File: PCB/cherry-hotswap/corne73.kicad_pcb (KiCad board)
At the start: 2 copper layers, 277.2 x 107.5 mm, 70 parts, among them J1 TYPE-C-31-M-13C, J2 TRS, J3 Conn_01x04, J4 Conn_01x03, SW1 SW_Push, SW10 SW_Push, SW11 SW_Push, SW12 SW_Push, SW13 SW_Push, SW14 SW_Push, SW15 SW_Push, SW16 SW_Push, SW17 SW_Push, SW18 SW_Push, SW19 SW_Push, SW2 SW_Push, SW20 SW_Push, SW21 SW_Push, SW3 SW_Push, SW4 SW_Push, SW5 SW_Push, SW6 SW_Push, SW7 SW_Push, SW8 SW_Push, SW9 SW_Push, U3 TPD4E05U06DQAR

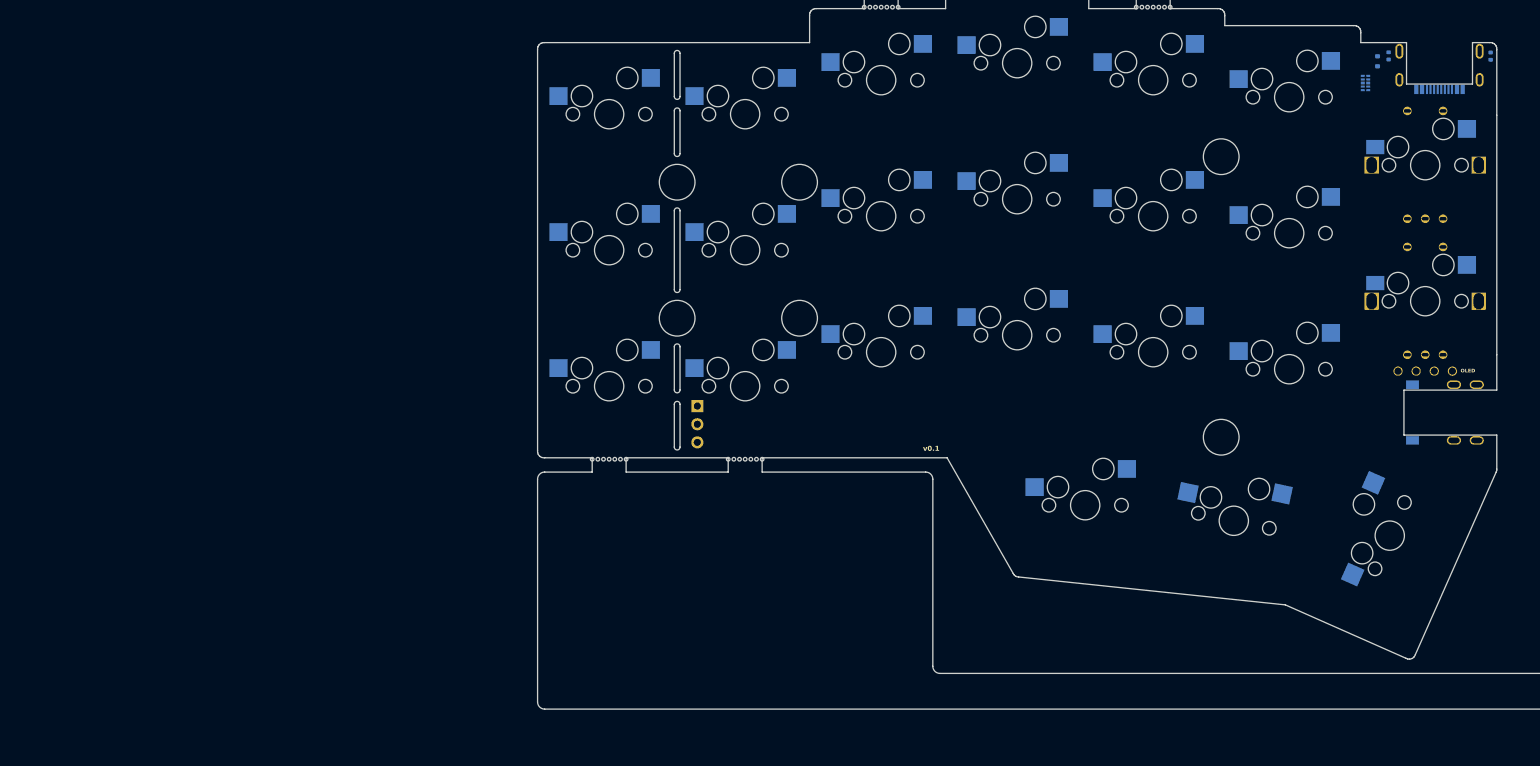
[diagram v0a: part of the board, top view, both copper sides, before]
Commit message: Initial left side components
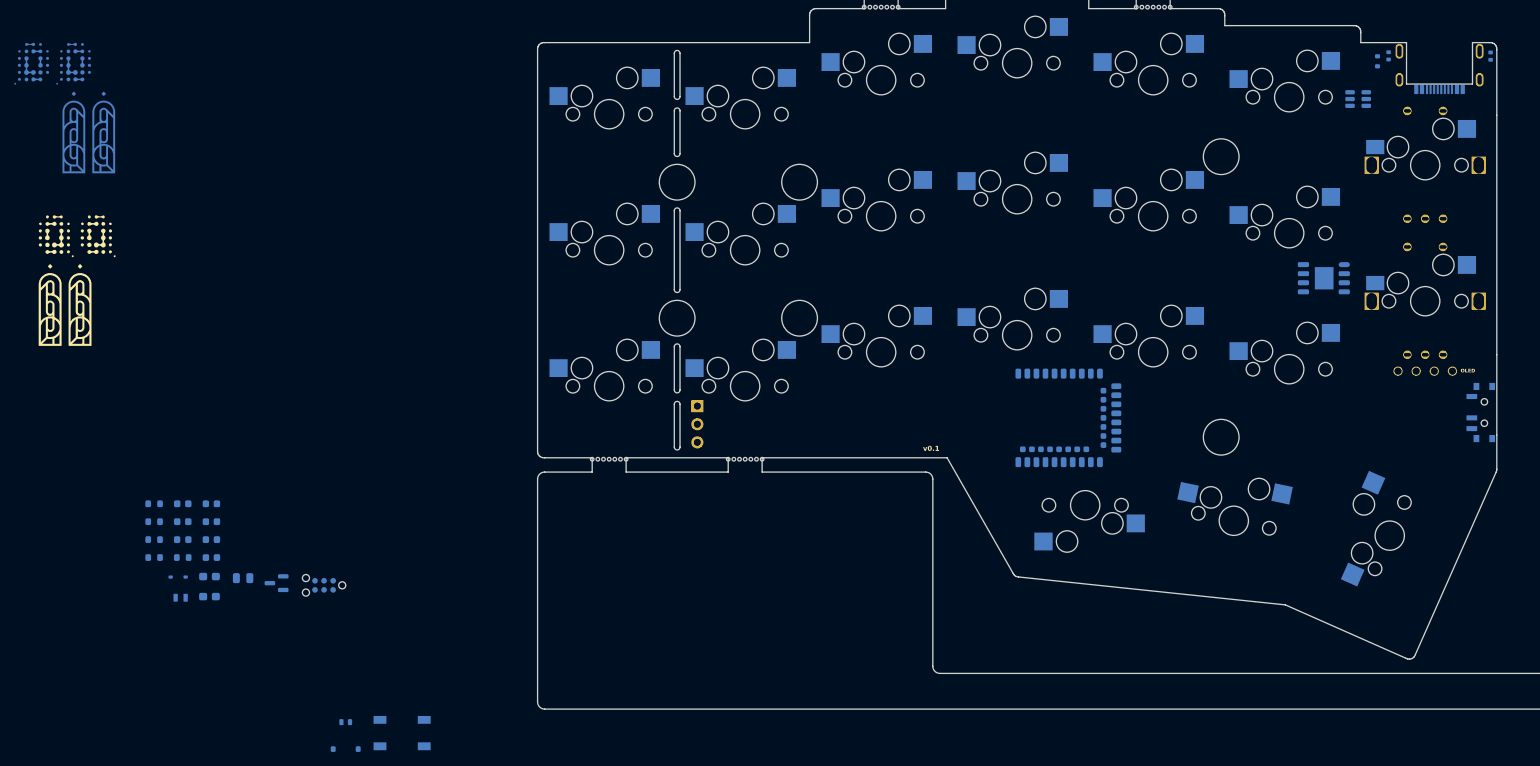
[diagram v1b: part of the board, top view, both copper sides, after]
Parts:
- removed J2: TRS, kbd_local:PJ-398A-5A_PJ-399B-6A
- added C1: 12p, Capacitor_SMD:C_0603_1608Metric, B.Cu at (-184.3, 47.4)
- added C2: 12p, Capacitor_SMD:C_0603_1608Metric, B.Cu at (-184.3, 49.9)
- added C3: 4.7u, Capacitor_SMD:C_0603_1608Metric, B.Cu at (-184.3, 52.4)
- added C4: 1u, Capacitor_SMD:C_0603_1608Metric, B.Cu at (-184.3, 55.0)
- added C5: 4.7u, Capacitor_SMD:C_0603_1608Metric, B.Cu at (-188.3, 47.4)
- added C6: 10uF, Capacitor_Tantalum_SMD:CP_EIA-2012-12_Kemet-R, B.Cu at (-184.6, 57.6)
- added C7: 4.7u, Capacitor_SMD:C_0603_1608Metric, B.Cu at (-188.3, 49.9)
- added C8: 10uF, Capacitor_Tantalum_SMD:CP_EIA-2012-12_Kemet-R, B.Cu at (-184.6, 60.4)
- added D1: Schottky, Diode_SMD:D_SOD-323, B.Cu at (-189.0, 57.7)
- added H1: qw-logo, qw-logo:qw new logo silk + copper sm, F.Cu at (-206.0, 9.95)
- added H2: qw-logo, qw-logo:qw new logo silk + copper sm, F.Cu at (-200.2, 9.95)
- added H3: qw-logo, qw-logo:qw new logo silk + copper sm, B.Cu at (-203.6, -14.2)
- added H4: qw-logo, qw-logo:qw new logo silk + copper sm, B.Cu at (-209.5, -14.2)
- added H5: 1999-logo, 1999:1999 logo md, F.Cu at (-207.1, 19.6)
- added H6: 1999-logo, 1999:1999 logo md, F.Cu at (-202.9, 19.6)
- added H7: 1999-logo, 1999:1999 logo md, B.Cu at (-199.2, -4.61)
- added H8: 1999-logo, 1999:1999 logo md, B.Cu at (-203.3, -4.61)
- added J5: TC2030_SWD, PCM_marbastlib-various:CON_TC2030_outlined, B.Cu at (-168.5, 58.8)
- added J6: Battery, Connector_Molex:Molex_Pico-EZmate_78171-0002_1x02-1MP_P1.20mm_Vertical, B.Cu at (-165.5, 79.9)
- added L1: 10 uH, Inductor_SMD:L_0603_1608Metric, B.Cu at (-188.3, 52.4)
- added LED1: CHARGE, LED_SMD:LED_0805_2012Metric, B.Cu at (-179.9, 57.8)
- added Q1: AO3401A, Package_TO_SOT_SMD:SOT-23, B.Cu at (-175.2, 58.5)
- added R3: 806, Resistor_SMD:R_0603_1608Metric, B.Cu at (-188.3, 55.0)
- added R4: 2M, Resistor_SMD:R_0603_1608Metric, B.Cu at (-192.3, 47.4)
- added R5: 10k, Resistor_SMD:R_0603_1608Metric, B.Cu at (-192.3, 49.9)
- added R6: 5k, Resistor_SMD:R_0603_1608Metric, B.Cu at (-192.3, 52.4)
- added R7: 5k, Resistor_SMD:R_0603_1608Metric, B.Cu at (-192.3, 55.0)
- added SW22: SW_SPDT, Button_Switch_SMD:SW_SPDT_PCM12, B.Cu at (-6.33, 34.6)
- added SW23: SW_Push, Button_Switch_SMD:SW_SPST_SKQG_WithStem, B.Cu at (-157.6, 79.5)
- added U1: nRF52840_E73-2G4M08S1C, PCM_marbastlib-various:nRF52840_E73-2G4M08S1C, B.Cu at (-66.3, 35.4)
- added U2: TP4056, qw-footprints:CustomTP4056, B.Cu at (-28.4, 15.8)
- added Y1: 32.768 KHz, Crystal:Crystal_SMD_2012-2Pin_2.0x1.2mm, B.Cu at (-188.6, 60.6)
- U3: value TPD4E05U06DQAR -> USBLC6-2SC6; footprint Package_SON:USON-10_2.5x1.0mm_P0.5mm -> Package_TO_SOT_SMD:SOT-23-6
- moved U3 2.47 mm to (-23.7, -9.26), turned to 180 degrees
- turned SW9 to 0 degrees
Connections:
- J1 pad A6: /left/D+ -> DBUS+
- J1 pad A7: /left/D- -> DBUS-
- J1 pad B6: /left/D+ -> DBUS+
- J1 pad B7: /left/D- -> DBUS-
- U3 pad 1: /left/D+ -> DBUS-
- U3 pad 2: /left/D- -> GND
- U3 pad 3: GND -> D-
- U3 pad 4: /left/D+ -> D+
- U3 pad 5: /left/D- -> +5V
- U3 pad 6: /left/D- -> DBUS+
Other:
- outline, holes or cut-outs redrawn
